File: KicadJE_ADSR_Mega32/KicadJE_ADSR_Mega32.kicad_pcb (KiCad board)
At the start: 2 copper layers, 100 x 100 mm, 134 parts, among them J101 ADSR1, J102 ADSR2, J103 ADSR1, J104 ADSR2, J105 ADSR1-G8, J106 ADSR2-G8, J107 ADSR4-G8, J108 ADSR3-G8, J201 AVR-ISP-6, J202 UART, J301 In, J302 +5V reg/doepfer, J303 Out, J304 CV_time, J305 CV doepfer, P101 Doepfer_Power_16pin, P302 Doepfer_Power_16pin, Q301 BC337, Q302 PZT2222A, U201 ATmega32A-AU, U301 L78L05_TO92, U302 PT2399, Y201 16MHz

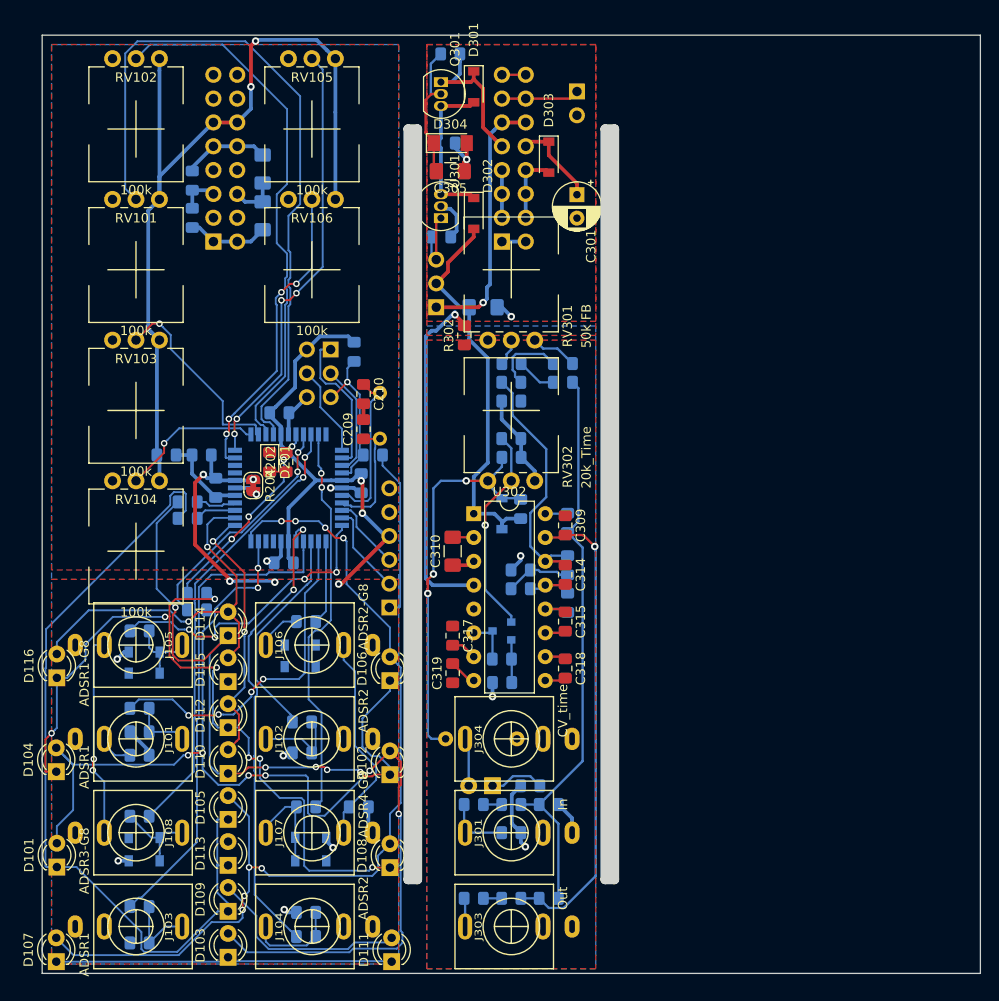
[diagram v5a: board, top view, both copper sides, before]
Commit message: ATMega32A routed
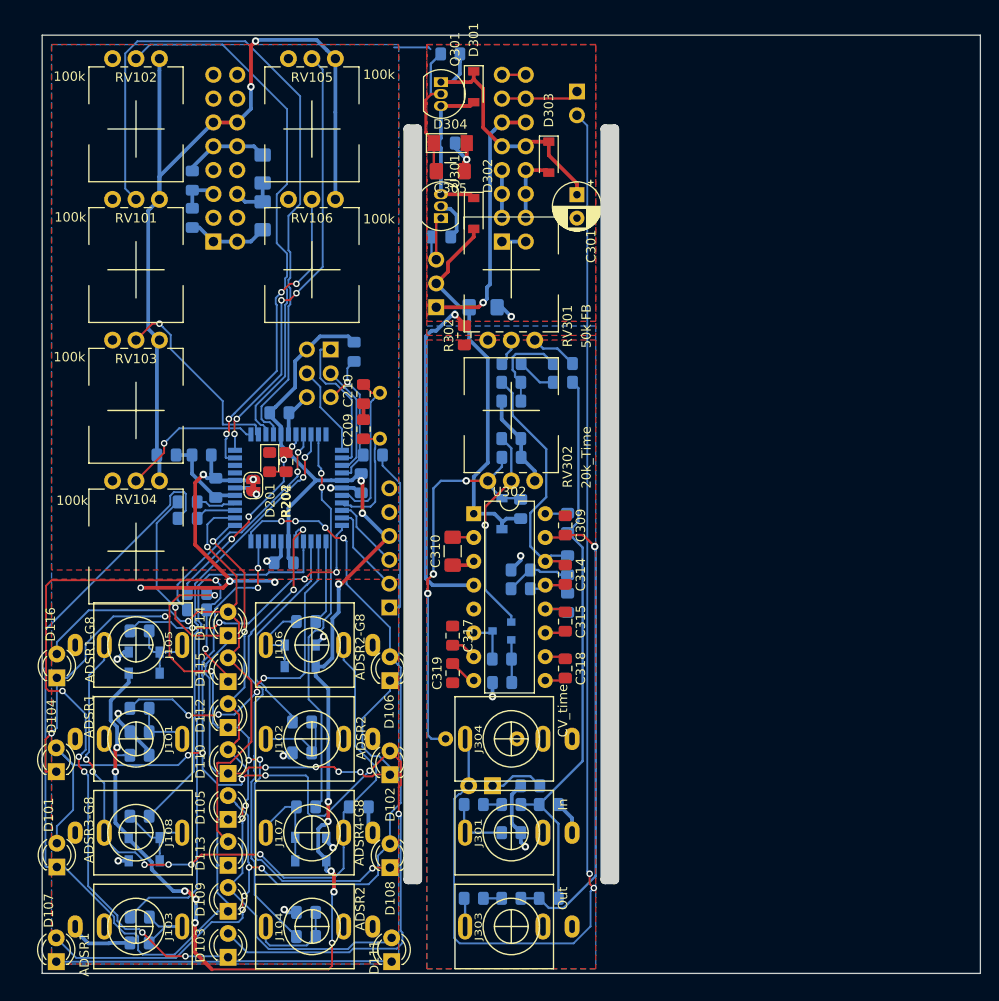
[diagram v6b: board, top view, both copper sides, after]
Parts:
- moved R113 1.13 mm to (60.4, 144.0)
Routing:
- net CV: track 5.16 -> 125.0 mm, vias 0 -> 2
- net +5V: track 175.1 -> 270.4 mm, vias 6 -> 16
- net Net-(D103-Pad1): track 36.1 -> 121.0 mm, vias 0 -> 7
- net Net-(J105-PadTN): track 44.5 -> 77.6 mm, vias 2 -> 6
- net 21: track 41.9 -> 65.3 mm
- net GNDA: track 66.4 -> 86.7 mm, vias 12 -> 15
- net 20: track 50.3 -> 66.7 mm, vias 2 -> 4
- net Net-(D102-Pad1): track 73.4 -> 68.9 mm
- net ADSR2-G8: track 4.69 -> 9.01 mm
- net (no net): track 0.00 -> 3.98 mm
- net 14_PWM: track 52.3 -> 56.2 mm
- net +12Vb: track 26.9 -> 29.5 mm
- net Net-(C312-Pad1): track 7.94 -> 9.94 mm
- net Net-(D104-Pad1): track 82.6 -> 84.4 mm
- net 10_INT0: track 31.8 -> 30.5 mm
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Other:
- board text added: "+5V"

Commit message: labeling
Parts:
- moved R204 6.07 mm to (67.4, 94.7), turned to 180 degrees
- moved Y201 2.40 mm to (86.0, 90.6)
- moved D302 1.97 mm to (96.8, 67.2)
- moved R205 1.65 mm to (83.2, 82.1)
- moved D201 0.11 mm to (74.2, 95.4)
- moved R202 0.10 mm to (76.0, 95.4)
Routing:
- net +5V: track 270.4 -> 300.6 mm
- net GND: track 86.8 -> 110.7 mm, vias 6 -> 7
- net /KicadJE-EU1-PT2399_sub/7v5: track 17.2 -> 22.0 mm
- net (no net): track 3.98 -> 0.00 mm
- net Net-(C209-Pad1): track 12.7 -> 16.5 mm
- net Net-(C210-Pad1): track 17.2 -> 19.9 mm
- net LFP1-In: track 2.40 -> 4.62 mm
- net +5VA: track 51.3 -> 53.4 mm
- net 0_LED: track 21.7 -> 23.6 mm
- net Net-(D201-Pad2): track 1.75 -> 0.00 mm
- net reset: track 16.5 -> 17.9 mm
- net 18: track 125.9 -> 126.7 mm
- net GNDA: track 86.7 -> 87.2 mm, vias 15 -> 14
- removed copper zone on F.Cu, net +5V
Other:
- board text added: "GND"

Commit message: Logo
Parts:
- added G***: LOGO, AJ:Johansen_engineering_logo_25mm_front_neg5, B.Cu at (53.0, 102.0)
- added G***: LOGO, AJ:Johansen_engineering_logo_25mm_front_neg5, F.Cu at (76.6, 107.1)
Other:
- board text added: "EU-4 Reverb"
- board text added: "EU-5 ADSR32"
- board text added: "Johansen Engineering ADSR Mega32 - Rev A - 2019 05 11"
- board text added: "Johansen Engineering PT2399 - Rev B 2019 05 11"
